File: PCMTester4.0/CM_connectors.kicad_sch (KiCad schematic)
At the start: 28 parts, among them J2 FX11A-80P8, J3 FX11A-80P8

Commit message: FINAL VERSION
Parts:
- removed C11, C12, C13, C14, C15, C16, C17: 470nF, Capacitor_SMD:C_0402_1005Metric, symbol Device:C
- removed J2: FX11A-80P8, Library:HIROSE_FX11A-80P-8-SV, symbol ECON:FX11A-80P8
- added DF1: DF12 connector for HGCAL test boards for partial 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, PCMFootprints:HRS_DF12NB-60DS-0.5V_51_, symbol DF12_symbol.schlib:root_0_DF12NB-60DS-0.5V_pCM_test.SCHLIB
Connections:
- net DERR2: no longer J3.1
- net ECOND_RE_SB: no longer J3.50
- net ECON_RE_HB: no longer J3.52
- net GND: now also DF1.11 (GND), DF1.17 (GND), DF1.23 (GND), DF1.29 (GND), DF1.35 (GND), DF1.41 (GND), DF1.47 (GND), DF1.5 (GND), DF1.50 (GND), DF1.53 (GND), DF1.56 (GND), DF1.59 (GND), DF1.6 (GND)
- net SCL: no longer J3.12
- net SDA: no longer J3.10
- net VDD: now also DF1.12 (P1V2D), DF1.14 (P1V2D), DF1.16 (P1V2D), DF1.18 (P1V2D), DF1.20 (P1V2D), DF1.22 (P1V2D), DF1.24 (P1V2D)
- net D.CLK320_N renamed ECON_D_DAQ_OUT_P
- net D.CLK320_P renamed ECON_D_DAQ_OUT_N
- net D.FCMD_N: no longer names the net of J3.6
- net D.FCMD_P: no longer names the net of J3.2
- net DAQ03N renamed BM28_VMON_LVS
- net DAQ03P renamed BM28_PWR_EN_LDL
- net DAQ04N renamed TEST_IO
- net DAQ04P renamed BM28_PG_LDO
- net DAQ05N renamed CLK320_IN_N
- net DAQ05P renamed CLK320_IN_P
- net DAQ06N renamed FCMD_IN_N
- net DAQ06P renamed FCMD_IN_P
- net DAQ_out00N renamed BM28_I2C_SDA
- net DAQ_out00P renamed ECON_D_ERROR_B
- net DAQ_out01N renamed ECON_D_RESET_B
- net DAQ_out01P renamed ECON_T_RESET_B
- net TRIG05N: no longer names the net of J3.78
- net TRIG05P: no longer names the net of J3.74
- net TRIG06N renamed BM28_RTD_REF
- net TRIG06P renamed MGND
- net TRIG07N: no longer names the net of J3.42
- net TRIG07P renamed BM28_S1_HGCROC_RE_SB
- net TRIG08N renamed ECON_D_SOFT_RESET_B
- net TRIG08P renamed ECON_T_SOFT_RESET_B
- net TRIG09N renamed ECON_T_TRIG_OUT_1_P
- net TRIG09P renamed ECON_T_TRIG_OUT_1_N
- net TRIG10N renamed ECON_T_TRIG_OUT_0_P
- net TRIG10P renamed ECON_T_TRIG_OUT_0_N
- net TRIG11N renamed TEST_0_N
- net TRIG11P renamed TEST_0_P
- net TRIG12N renamed BM28_RTD
- net TRIG12P renamed BM28_PROBE_DC
- new net BM28_HGCROC_RE_HB: J3.52
- new net BM28_I2C_SCL: J3.12
- new net BM28_S2_HGCROC_RE_SB: J3.50
- new net HGCROC_RE_HB: DF1.32 (HGCROC_RE_HB)
- new net I2C_SCL: DF1.8 (I2C_SCL)
- new net I2C_SDA: DF1.10 (I2C_SDA)
- new net PG_LDO: DF1.34 (PG_LDO)
- new net PWR_EN_LDO: DF1.38 (PWR_EN_LDO)
- new net RTD: DF1.46 (RTD)
- new net RTD_REF: DF1.48 (RTD_REF)
- new net S1_CLK320_N: DF1.45 (S1_CLK320_N)
- new net S1_CLK320_P: DF1.43 (S1_CLK320_P)
- new net S1_DAQ_X0_N: DF1.57 (S1_DAQ_X0_N)
- new net S1_DAQ_X0_P: DF1.55 (S1_DAQ_X0_P)
- new net S1_DAQ_X1_N: DF1.37 (S1_DAQ_X1_N)
- new net S1_DAQ_X1_P: DF1.39 (S1_DAQ_X1_P)
- new net S1_ERR: DF1.44 (S1_ERR)
- new net S1_FCMD_N: DF1.51 (S1_FCMD_N)
- new net S1_FCMD_P: DF1.49 (S1_FCMD_P)
- new net S1_HGCROC_RE_SB: DF1.40 (S1_HGCROC_RE_SB)
- new net S1_PROBE_DC: DF1.42 (S1_PROBE_DC)
- new net S1_TRIG_0_N: DF1.58 (S1_TRIG_0_N)
- new net S1_TRIG_0_P: DF1.60 (S1_TRIG_0_P)
- new net S1_TRIG_1_N: DF1.52 (S1_TRIG_1_N)
- new net S1_TRIG_1_P: DF1.54 (S1_TRIG_1_P)
- new net S1_TRIG_2_N: DF1.31 (S1_TRIG_2_N)
- new net S1_TRIG_2_P: DF1.33 (S1_TRIG_2_P)
- new net S1_TRIG_3_N: DF1.25 (S1_TRIG_3_N)
- new net S1_TRIG_3_P: DF1.27 (S1_TRIG_3_P)
- new net S2_CLK320_N: DF1.3 (S2_CLK320_N)
- new net S2_CLK320_P: DF1.1 (S2_CLK320_P)
- new net S2_DAQ_X0_N: DF1.15 (S2_DAQ_X0_N)
- new net S2_DAQ_X0_P: DF1.13 (S2_DAQ_X0_P)
- new net S2_ERR: DF1.26 (S2_ERR)
- new net S2_FCMD_N: DF1.9 (S2_FCMD_N)
- new net S2_FCMD_P: DF1.7 (S2_FCMD_P)
- new net S2_HGCROC_RE_SB: DF1.30 (S2_HGCROC_RE_SB)
- new net S2_PROBE_DC: DF1.28 (S2_PROBE_DC)
- new net S2_TRIG_0_N: DF1.21 (S2_DAQ_X0_N)
- new net S2_TRIG_0_P: DF1.19 (S2_TRIG_0_P)
- new net S2_TRIG_1_N: DF1.4 (S2_TRIG_1_N)
- new net S2_TRIG_1_P: DF1.2 (S2_TRIG_1_P)
- new net VMON_LVS: DF1.36 (VMON_LVS)
- no-connect marks 3 -> 2
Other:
- moved on the sheet: C1, C10, C18, C19, C2, C20, C21, C3, C4, C5, C6, C7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

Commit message: ts buss
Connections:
- net I2C_SCL is gone; now on net SCL: DF1.8 (I2C_SCL)
- net I2C_SDA is gone; now on net SDA: DF1.10 (I2C_SDA)

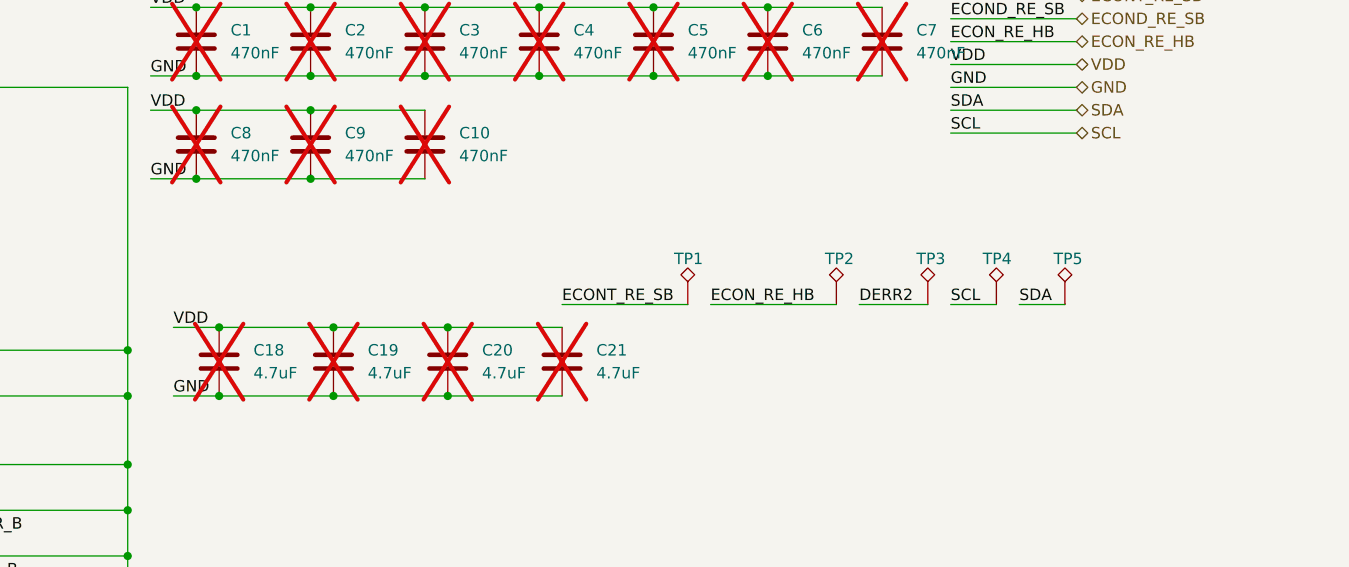
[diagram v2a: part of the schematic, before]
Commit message: added ground and power (w/ jumpers) planes as well as all the ground and power conn. and the capacitors. Also added half of the mounting holes
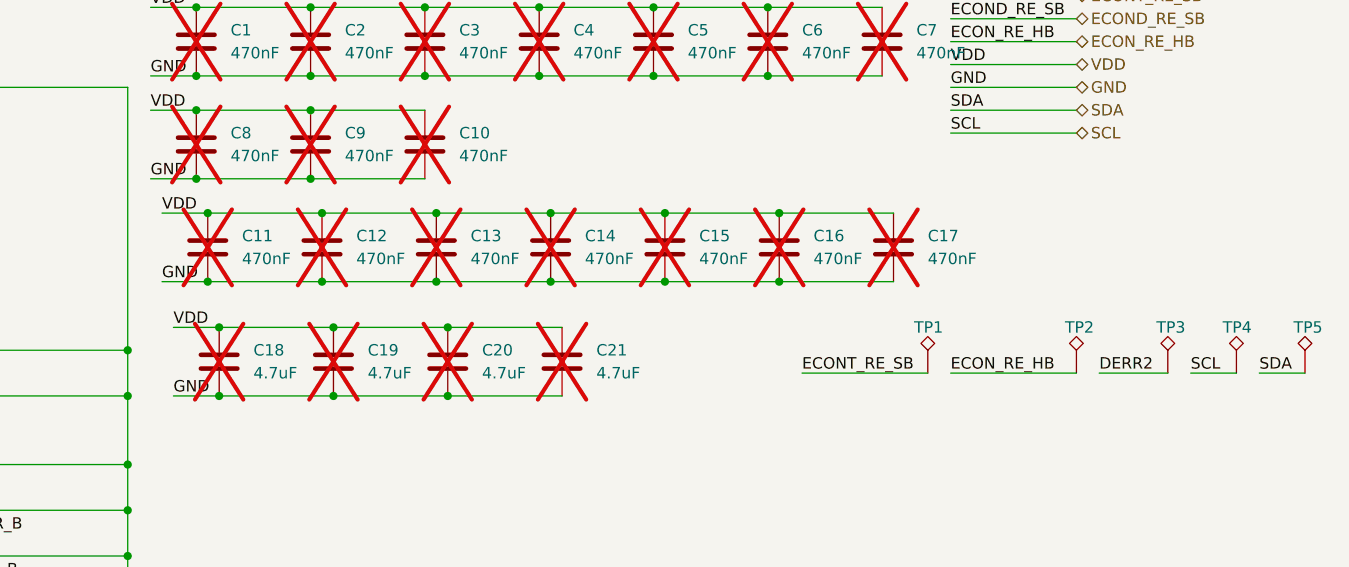
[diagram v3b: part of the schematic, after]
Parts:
- added C11, C12, C13, C14, C15, C16, C17: 470nF, Capacitor_SMD:C_0402_1005Metric, symbol Device:C
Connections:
- net GND: now also C11.2, C12.2, C13.2, C14.2, C15.2, C16.2, C17.2
- net VDD: now also C11.1, C12.1, C13.1, C14.1, C15.1, C16.1, C17.1
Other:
- moved on the sheet: TP1, TP2, TP3, TP4, TP5
